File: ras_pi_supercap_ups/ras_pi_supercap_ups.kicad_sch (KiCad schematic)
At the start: 67 parts, among them J3 Conn_01x05, J4 Conn_01x05, J6 Conn_01x04, J7 Conn_01x04, J8 Conn_02x03_Odd_Even, J9 LEDs and Buttons, Q1 IRF5305, U1 KA431AZTA, U2 KA431AZTA, U3 KA431AZTA, U4 KA431AZTA, U5 KA431AZTA, U6 LM2596S-5, U7 L7805, U8 ATtiny85-20P, U9 STC8H1K08

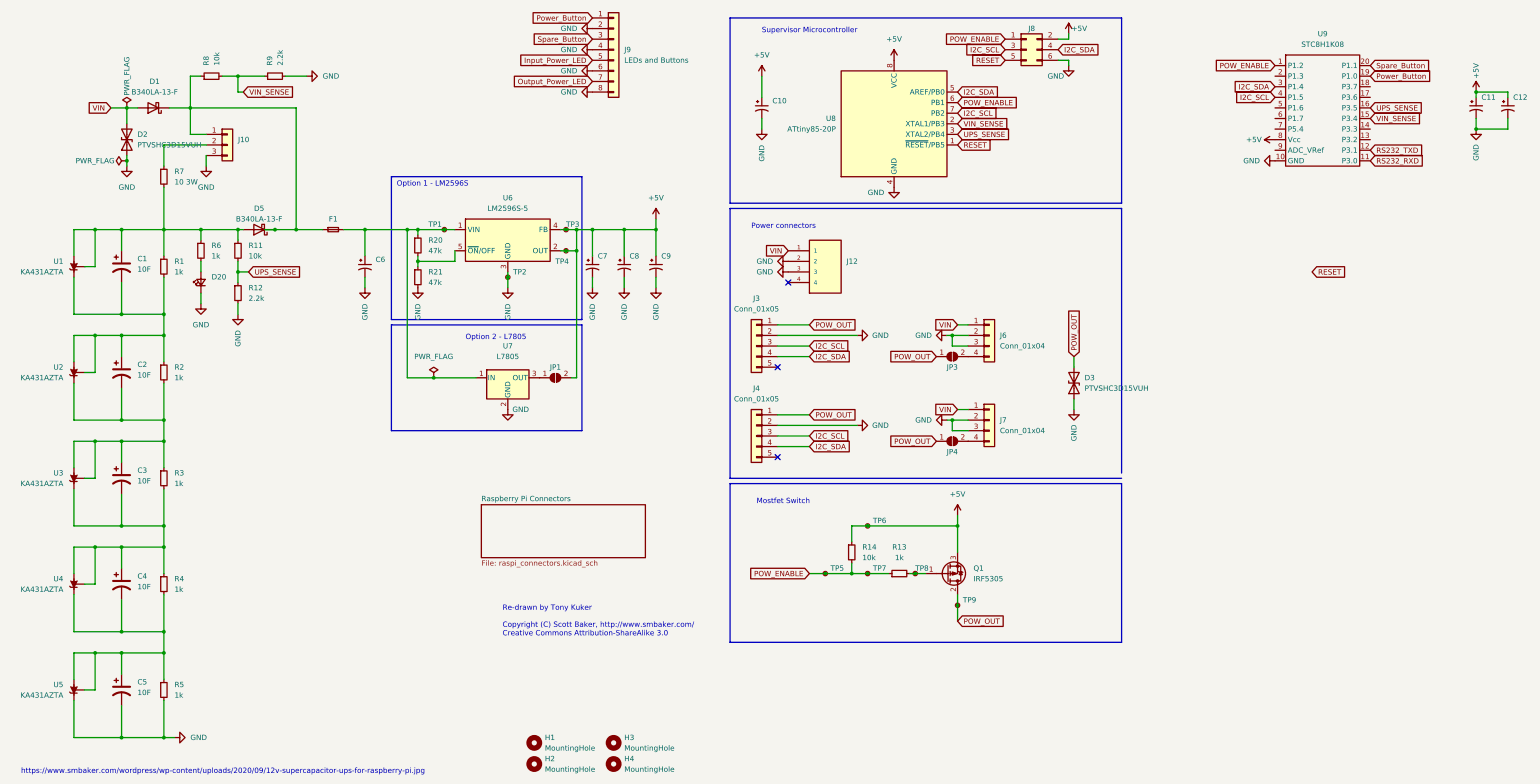
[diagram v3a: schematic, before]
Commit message: Added simple buck converter
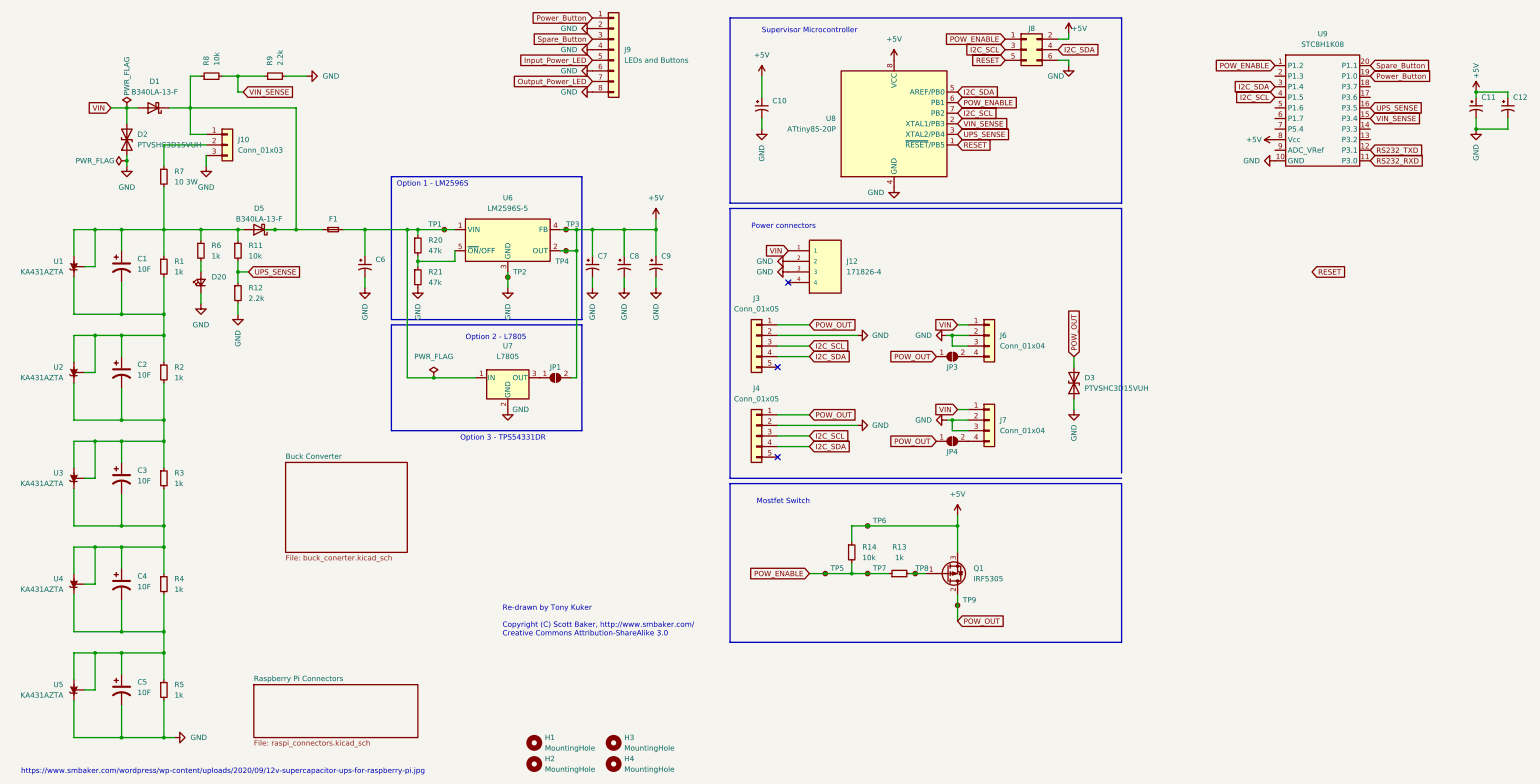
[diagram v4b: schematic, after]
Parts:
- J10: value (none) -> Conn_01x03; footprint (none) -> Connector_PinHeader_2.54mm:PinHeader_1x03_P2.54mm_Vertical
- J12: value (none) -> 171826-4; footprint (none) -> TE_171826-4
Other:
- added sheet Buck Converter (buck_conerter.kicad_sch)
- note added: "Option 3 - TPS54331DR"
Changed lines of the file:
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@@
+    (effects (font (size 1.27 1.27)) (justify left bottom))
+  )
+  (text "Option 3 - TPS54331DR" (at 121.92 115.57 0)
     (effects (font (size 1.27 1.27)) (justify left bottom))
   )
@@
       (effects (font (size 1.27 1.27)) (justify left))
     )
-    (property "Value" "" (id 1) (at 68.58 45.7199 0)
-      (effects (font (size 1.27 1.27)) (justify left))
-    )
-    (property "Footprint" "" (id 2) (at 66.04 44.45 0)
+    (property "Value" "Conn_01x03" (id 1) (at 68.58 45.7199 0)
+      (effects (font (size 1.27 1.27)) (justify left))
+    )
+    (property "Footprint" "Connector_PinHeader_2.54mm:PinHeader_1x03_P2.54mm_Vertical" (id 2) (at 66.04 44.45 0)
       (effects (font (size 1.27 1.27)) hide)
     )
@@
       (effects (font (size 1.27 1.27)) (justify left))
     )
-    (property "Value" "" (id 1) (at 214.63 74.9299 0)
-      (effects (font (size 1.27 1.27)) (justify left))
-    )
-    (property "Footprint" "" (id 2) (at 210.82 74.93 0)
+    (property "Value" "171826-4" (id 1) (at 214.63 74.9299 0)
+      (effects (font (size 1.27 1.27)) (justify left))
+    )
+    (property "Footprint" "TE_171826-4" (id 2) (at 210.82 74.93 0)
       (effects (font (size 1.27 1.27)) (justify left bottom) hide)
     )
@@
     )
   )
-  (sheet (at 127 130.81) (size 39.37 12.7) (fields_autoplaced)
+  (sheet (at 80.01 120.65) (size 29.21 21.59) (fields_autoplaced)
     (stroke (width 0.1524) (type solid) (color 0 0 0 0))
     (fill (color 0 0 0 0.0000))
-    (property "Sheet name" "Raspberry Pi Connectors" (id 0) (at 127 130.0984 0)
+    (property "Sheet name" "Buck Converter" (id 0) (at 80.01 119.9384 0)
       (effects (font (size 1.27 1.27)) (justify left bottom))
     )
-    (property "Sheet file" "raspi_connectors.kicad_sch" (id 1) (at 127 144.0946 0)
+    (property "Sheet file" "buck_conerter.kicad_sch" (id 1) (at 80.01 142.8246 0)
+      (effects (font (size 1.27 1.27)) (justify left top))
+    )
+  )
+  (sheet (at 72.39 173.99) (size 39.37 12.7) (fields_autoplaced)
+    (stroke (width 0.1524) (type solid) (color 0 0 0 0))
+    (fill (color 0 0 0 0.0000))
+    (property "Sheet name" "Raspberry Pi Connectors" (id 0) (at 72.39 173.2784 0)
+      (effects (font (size 1.27 1.27)) (justify left bottom))
+    )
+    (property "Sheet file" "raspi_connectors.kicad_sch" (id 1) (at 72.39 187.2746 0)
       (effects (font (size 1.27 1.27)) (justify left top))
     )
@@
     (path "/" (page "1"))
     (path "/c783ab4c-6f9b-478c-bda9-be5294b6d6a7" (page "2"))
+    (path "/90ba58c0-bb86-40e1-a3eb-4c6438e0a945" (page "3"))
   )
   (symbol_instances
@@
       (reference "#PWR0106") (unit 1) (value "GND") (footprint "")
     )
+    (path "/90ba58c0-bb86-40e1-a3eb-4c6438e0a945/e6ce3ddf-4520-4405-8108-ba1655fba88d"
+      (reference "#PWR0107") (unit 1) (value "GND") (footprint "")
+    )
+    (path "/90ba58c0-bb86-40e1-a3eb-4c6438e0a945/8198a8aa-a634-460a-b21c-b6a77ff2cbfb"
+      (reference "#PWR0108") (unit 1) (value "GND") (footprint "")
+    )
+    (path "/90ba58c0-bb86-40e1-a3eb-4c6438e0a945/27adb203-718d-444a-8040-f884266928ac"
+      (reference "#PWR0109") (unit 1) (value "GND") (footprint "")
+    )
+    (path "/90ba58c0-bb86-40e1-a3eb-4c6438e0a945/43879ac7-f230-4696-95ed-6babb22f0407"
+      (reference "#PWR0110") (unit 1) (value "GND") (footprint "")
+    )
+    (path "/90ba58c0-bb86-40e1-a3eb-4c6438e0a945/85ee7195-de50-4114-be45-19560de38bf5"
+      (reference "#PWR0111") (unit 1) (value "GND") (footprint "")
+    )
+    (path "/90ba58c0-bb86-40e1-a3eb-4c6438e0a945/459b2b91-449a-44df-86b2-6ea6b0ec5f29"
+      (reference "#PWR0112") (unit 1) (value "GND") (footprint "")
+    )
     (path "/f3b0a20e-4c8e-4cdd-b600-0f64fa0e367b"
       (reference "C1") (unit 1) (value "10F") (footprint "Capacitor_THT:CP_Radial_D12.5mm_P5.00mm")
@@
       (reference "C12") (unit 1) (value "0.1uF") (footprint "Capacitor_SMD:C_0805_2012Metric")
     )
+    (path "/90ba58c0-bb86-40e1-a3eb-4c6438e0a945/1aee80e0-d5ab-4041-a69f-25c9526af2c9"
+      (reference "C101") (unit 1) (value "4.7u") (footprint "Capacitor_SMD:C_0805_2012Metric")
+    )
+    (path "/90ba58c0-bb86-40e1-a3eb-4c6438e0a945/7f290db6-baca-4c3e-b3ab-eccf38ab3ab8"
+      (reference "C102") (unit 1) (value "4.7u") (footprint "Capacitor_SMD:C_0805_2012Metric")
+    )
+    (path "/90ba58c0-bb86-40e1-a3eb-4c6438e0a945/d386a4ed-6f5f-41e0-bd59-e257d591d691"
+      (reference "C103") (unit 1) (value "0.01u") (footprint "Capacitor_SMD:C_0805_2012Metric")
+    )
+    (path "/90ba58c0-bb86-40e1-a3eb-4c6438e0a945/4d1de5fc-63eb-4508-a6cb-5dfbce2f9c27"
+      (reference "C104") (unit 1) (value "0.1u") (footprint "Capacitor_SMD:C_0805_2012Metric")
+    )
+    (path "/90ba58c0-bb86-40e1-a3eb-4c6438e0a945/9214c3d8-8058-4003-977f-8d150c662226"
+      (reference "C105") (unit 1) (value "0.01u") (footprint "Capacitor_SMD:C_0805_2012Metric")
+    )
+    (path "/90ba58c0-bb86-40e1-a3eb-4c6438e0a945/45663991-efaa-4bf4-9634-0270f1f3793d"
+      (reference "C106") (unit 1) (value "1000p") (footprint "Capacitor_SMD:C_0805_2012Metric")
+    )
+    (path "/90ba58c0-bb86-40e1-a3eb-4c6438e0a945/51bf57bb-586e-41c7-b39c-b7a9940bcccf"
+      (reference "C107") (unit 1) (value "47p") (footprint "Capacitor_SMD:C_0805_2012Metric")
+    )
+    (path "/90ba58c0-bb86-40e1-a3eb-4c6438e0a945/88e71f15-52d0-4bd9-8ee2-a11f1c4fae0f"
+      (reference "C108") (unit 1) (value "47u") (footprint "Capacitor_SMD:C_0805_2012Metric")
+    )
+    (path "/90ba58c0-bb86-40e1-a3eb-4c6438e0a945/369f5296-8766-4702-957b-6c6122f23c3c"
+      (reference "C109") (unit 1) (value "47u") (footprint "Capacitor_SMD:C_0805_2012Metric")
+    )
     (path "/0d33a0a3-6701-41b8-8040-7340c4d8cd33"
       (reference "D1") (unit 1) (value "B340LA-13-F") (footprint "Diode_SMD:D_SMA")
@@
       (reference "D20") (unit 1) (value "Green") (footprint "LED_SMD:LED_0805_2012Metric")
     )
+    (path "/90ba58c0-bb86-40e1-a3eb-4c6438e0a945/b4776be9-846e-4f7b-8000-c86b979502bd"
+      (reference "D101") (unit 1) (value "B340A") (footprint "Diode_SMD:D_SMA")
+    )
     (path "/ad7143b5-340a-4af7-889c-efa5a5b701b0"
       (reference "F1") (unit 1) (value "Fuse_Small") (footprint "Fuse:Fuse_1206_3216Metric")
@@
     )
     (path "/c783ab4c-6f9b-478c-bda9-be5294b6d6a7/fc81ca8f-df1f-49ee-b900-486b8ee17f48"
-      (reference "J1") (unit 1) (value "Raspberry_Pi_2_3") (footprint "Connector_PinSocket_2.54mm:PinSocket_2x20_P2.54mm_Vertical")
+      (reference "J1") (unit 1) (value "Raspberry_Pi_2_3") (footprint "")
     )
     (path "/c783ab4c-6f9b-478c-bda9-be5294b6d6a7/9b50deac-a15e-4279-8964-578c1305abe5"
-      (reference "J2") (unit 1) (value "Raspberry_Pi_2_3") (footprint "Connector_PinSocket_2.54mm:PinSocket_2x20_P2.54mm_Vertical")
+      (reference "J2") (unit 1) (value "Raspberry_Pi_2_3") (footprint "")
     )
     (path "/801da5bf-4bc0-4304-a810-8e7ca96cd81e"
@@
       (reference "JP4") (unit 1) (value "SolderJumper_2_Open") (footprint "Jumper:SolderJumper-2_P1.3mm_Open_RoundedPad1.0x1.5mm")
     )
+    (path "/90ba58c0-bb86-40e1-a3eb-4c6438e0a945/7b0d2f0b-642a-441b-8802-b4d4fe4198d3"
+      (reference "L101") (unit 1) (value "6.8uH") (footprint "Inductor_SMD:L_6.3x6.3_H3")
+    )
     (path "/132098bb-22d7-46df-8f43-55471e68e57a"
       (reference "Q1") (unit 1) (value "IRF5305") (footprint "Package_TO_SOT_SMD:TO-263-2")
@@
       (reference "R21") (unit 1) (value "47k") (footprint "Resistor_SMD:R_0805_2012Metric")
     )
+    (path "/90ba58c0-bb86-40e1-a3eb-4c6438e0a945/403438b4-fc93-4243-82bc-3a27f53097d0"
+      (reference "R101") (unit 1) (value "332k") (footprint "Resistor_SMD:R_0805_2012Metric")
+    )
+    (path "/90ba58c0-bb86-40e1-a3eb-4c6438e0a945/2e07edd4-3513-42be-914c-012ab28f0b65"
+      (reference "R102") (unit 1) (value "68.1k") (footprint "Resistor_SMD:R_0805_2012Metric")
+    )
+    (path "/90ba58c0-bb86-40e1-a3eb-4c6438e0a945/2321c361-f940-46f4-bf53-78d84a432824"
+      (reference "R103") (unit 1) (value "29.4k") (footprint "Resistor_SMD:R_0805_2012Metric")
+    )
+    (path "/90ba58c0-bb86-40e1-a3eb-4c6438e0a945/8f1af006-b4f9-4d27-897d-093910fc650f"
+      (reference "R104") (unit 1) (value "0") (footprint "Resistor_SMD:R_0805_2012Metric")
+    )
+    (path "/90ba58c0-bb86-40e1-a3eb-4c6438e0a945/94614162-ac83-46a8-9bcf-e0257f48e678"
+      (reference "R105") (unit 1) (value "10.2k") (footprint "Resistor_SMD:R_0805_2012Metric")
+    )
+    (path "/90ba58c0-bb86-40e1-a3eb-4c6438e0a945/a1816a33-27f8-4d1d-bc90-431b78c69efc"
+      (reference "R106") (unit 1) (value "3.24k") (footprint "Resistor_SMD:R_0805_2012Metric")
+    )
     (path "/b0a2a0f7-05d9-4df6-b2d4-a22f4c69bbff"
       (reference "TP1") (unit 1) (value "TestPoint_Small") (footprint "TestPoint:TestPoint_THTPad_D2.0mm_Drill1.0mm")
@@
       (reference "U9") (unit 1) (value "STC8H1K08") (footprint "Package_SO:TSSOP-20_4.4x5mm_P0.5mm")
     )
-  )
+    (path "/90ba58c0-bb86-40e1-a3eb-4c6438e0a945/a79ca793-b460-4b18-a91b-9f80075c3273"
+      (reference "U10") (unit 1) (value "TPS54331DR") (footprint "SOIC127P599X175-8N")
+    )
+  )

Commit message: added 3d model
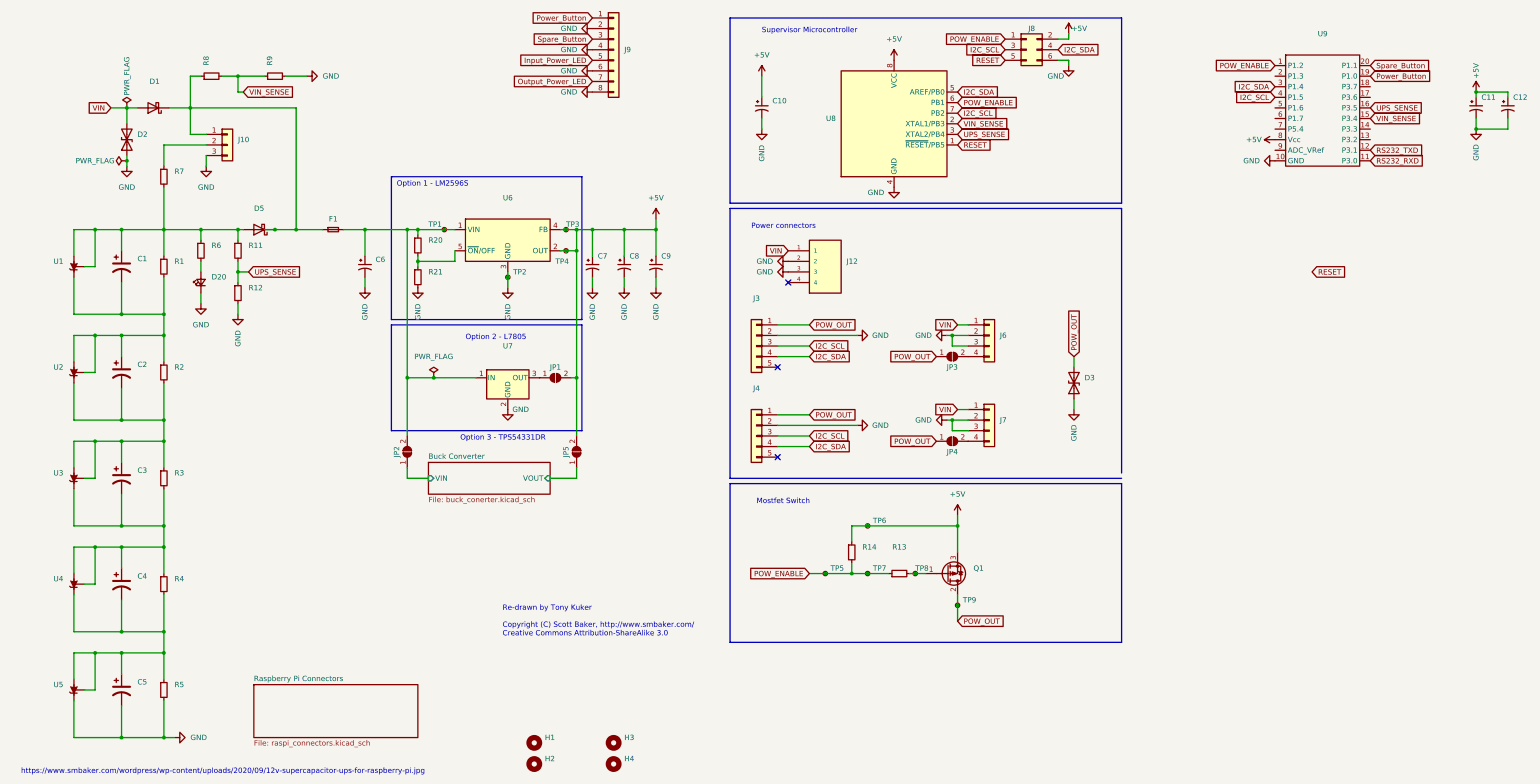
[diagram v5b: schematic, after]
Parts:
- added JP2, JP5: (no value), symbol Jumper:SolderJumper_2_Open
- C1, C2, C3, C4, C5: value 10F -> (none); footprint Capacitor_THT:CP_Radial_D12.5mm_P5.00mm -> (none)
- C10, C11, C7, C8, C9: value 22u 10V X7R -> (none); footprint Capacitor_SMD:C_0805_2012Metric -> (none)
- C12: value 0.1uF -> (none); footprint Capacitor_SMD:C_0805_2012Metric -> (none); LCSC C49678 -> C28233
- C6: value 10u 25V X7R -> (none); footprint Capacitor_SMD:C_0805_2012Metric -> (none)
- D1, D5: value B340LA-13-F -> (none); footprint Diode_SMD:D_SMA -> (none)
- D2, D3: value PTVSHC3D15VUH -> (none); footprint Diode_SMD:D_SOD-323 -> (none)
- D20: value Green -> (none); footprint LED_SMD:LED_0805_2012Metric -> (none); LCSC (none) -> C2293
- F1: value Fuse_Small -> (none); footprint Fuse:Fuse_1206_3216Metric -> (none)
- H1, H2, H3, H4: value MountingHole -> (none); footprint MountingHole:MountingHole_2.7mm_M2.5 -> (none)
- J10: value Conn_01x03 -> (none); footprint Connector_PinHeader_2.54mm:PinHeader_1x03_P2.54mm_Vertical -> (none)
- J12: value 171826-4 -> (none); footprint TE_171826-4 -> (none)
- J3, J4: value Conn_01x05 -> (none); footprint Connector_PinHeader_2.54mm:PinHeader_1x05_P2.54mm_Vertical -> (none)
- J6, J7: value Conn_01x04 -> (none); footprint Connector_PinHeader_2.54mm:PinHeader_1x04_P2.54mm_Vertical -> (none)
- J8: value Conn_02x03_Odd_Even -> (none); footprint Connector_PinHeader_2.54mm:PinHeader_2x03_P2.54mm_Vertical -> (none)
- J9: value LEDs and Buttons -> (none); footprint Connector_PinHeader_2.54mm:PinHeader_1x08_P2.54mm_Vertical -> (none)
- JP1, JP3, JP4: value SolderJumper_2_Open -> (none); footprint Jumper:SolderJumper-2_P1.3mm_Open_RoundedPad1.0x1.5mm -> (none)
- Q1: value IRF5305 -> (none); footprint Package_TO_SOT_SMD:TO-263-2 -> (none)
- R1, R2, R3, R4, R5: value 1k -> (none); footprint Resistor_SMD:R_1206_3216Metric -> (none)
- R11, R14, R8: value 10k -> (none); footprint Resistor_SMD:R_0805_2012Metric -> (none)
- R12, R9: value 2.2k -> (none); footprint Resistor_SMD:R_0805_2012Metric -> (none)
- R13, R6: value 1k -> (none); footprint Resistor_SMD:R_0805_2012Metric -> (none)
- R20, R21: value 47k -> (none); footprint Resistor_SMD:R_0805_2012Metric -> (none)
- R7: value 10 3W -> (none); footprint Resistor_THT:R_Axial_DIN0516_L15.5mm_D5.0mm_P25.40mm_Horizontal -> (none)
- TP1, TP2, TP3, TP4, TP5, TP6, TP7, TP8, TP9: value TestPoint_Small -> (none); footprint TestPoint:TestPoint_THTPad_D2.0mm_Drill1.0mm -> (none)
- U1, U2, U3, U4, U5: value KA431AZTA -> (none); footprint Package_TO_SOT_THT:TO-92_Inline -> (none)
- U6: value LM2596S-5 -> (none); footprint Package_TO_SOT_SMD:TO-263-5_TabPin3 -> (none)
- U7: value L7805 -> (none); footprint Package_TO_SOT_THT:TO-220-3_Vertical -> (none)
- U8: value ATtiny85-20P -> (none); footprint Package_DIP:DIP-8_W7.62mm -> (none)
- U9: value STC8H1K08 -> (none); footprint Package_SO:TSSOP-20_4.4x5mm_P0.5mm -> (none)
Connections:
- net +5V: now also JP5.2 (B)
- net at C6.1, F1.2, R20.1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: now also JP2.2 (B)
- new net Buck Converter/VIN: JP2.1 (A)
- new net Buck Converter/VOUT: JP5.1 (A)
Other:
- sheet Buck Converter ports: added VIN, VOUT; removed none
